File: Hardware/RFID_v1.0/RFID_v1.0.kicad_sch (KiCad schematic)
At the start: 0 parts

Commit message: RFID board schematic done, antenna head created in the layout
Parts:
- added C1, C4: 0.1uF, symbol device:C_Small
- added C10, C9: 180pF, symbol device:C_Small
- added C11, C12: 10pF, symbol device:C_Small
- added C13: 0.1uF, symbol Device:C_Small
- added C2, C3, C7, C8: 15pF, symbol device:C_Small
- added C5, C6: 47pF, symbol device:C_Small
- added J1: Conn_01x08, symbol Connector_Generic:Conn_01x08
- added L1, L2: 2.2uH, symbol Device:L
- added R1: 10k, symbol device:R_US
- added R2: 820R, symbol device:R_US
- added R3: 5k, symbol device:R_US
- added U1: MFRC52202HN1, HVQFN32_5X5_NXP, symbol MFRC52202HN1:MFRC52202HN1
- added Y1: XRCGB27M120F3G00R0, XRCGB27M120F3G00R0:OSC_XRCGB27M120F3G00R0, symbol XRCGB27M120F3G00R0:XRCGB27M120F3G00R0
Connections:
- new net: C4.1, R3.2
- new net: C10.1, C10.2, C11.1, C11.2, C12.1, C12.2, C4.2, C7.2, C8.2, C9.1, C9.2
- new net: C5.2, C7.1, L1.2
- new net: C6.1, C8.1, L2.2
- new net: C2.1, U1.22 (OSCOUT), Y1.3
- new net: C3.1, U1.21 (OSCIN), Y1.1
- new net +3V3: C13.1, J1.1 (Pin_1), R1.1, U1.12 (TVDD), U1.15 (AVDD), U1.2 (PVDD), U1.3 (DVDD), U1.32 (EA), U1.33 (EPAD)
- new net GND: C1.2, C13.2, C2.2, C3.2, C5.1, C6.2, J1.3 (Pin_3), U1.1 (I2C), U1.10 (TVSS), U1.14 (TVSS), U1.18 (AVSS), U1.4 (DVSS), U1.5 (PVSS)
- new net MISO: J1.5 (Pin_5), U1.31 (D7/SCL/MISO/TX)
- new net MOSI: J1.6 (Pin_6), U1.30 (D6/ADR_0/MOSI/MX)
- new net RST: J1.2 (Pin_2), R1.2, U1.6 (NRSTPD)
- new net RX: R2.2, R3.1, U1.17 (RX)
- new net SCK: J1.7 (Pin_7), U1.29 (D5/ADR_1/SCK/DTRQ)
- new net SDA: J1.8 (Pin_8), U1.24 (SDA/NSS/RX)
- new net TX1: L1.1, U1.11 (TX1)
- new net TX2: L2.1, U1.13 (TX2)
- new net Vmid: C1.1, R2.1, U1.16 (VMID)
- no-connect marks 0 -> 11

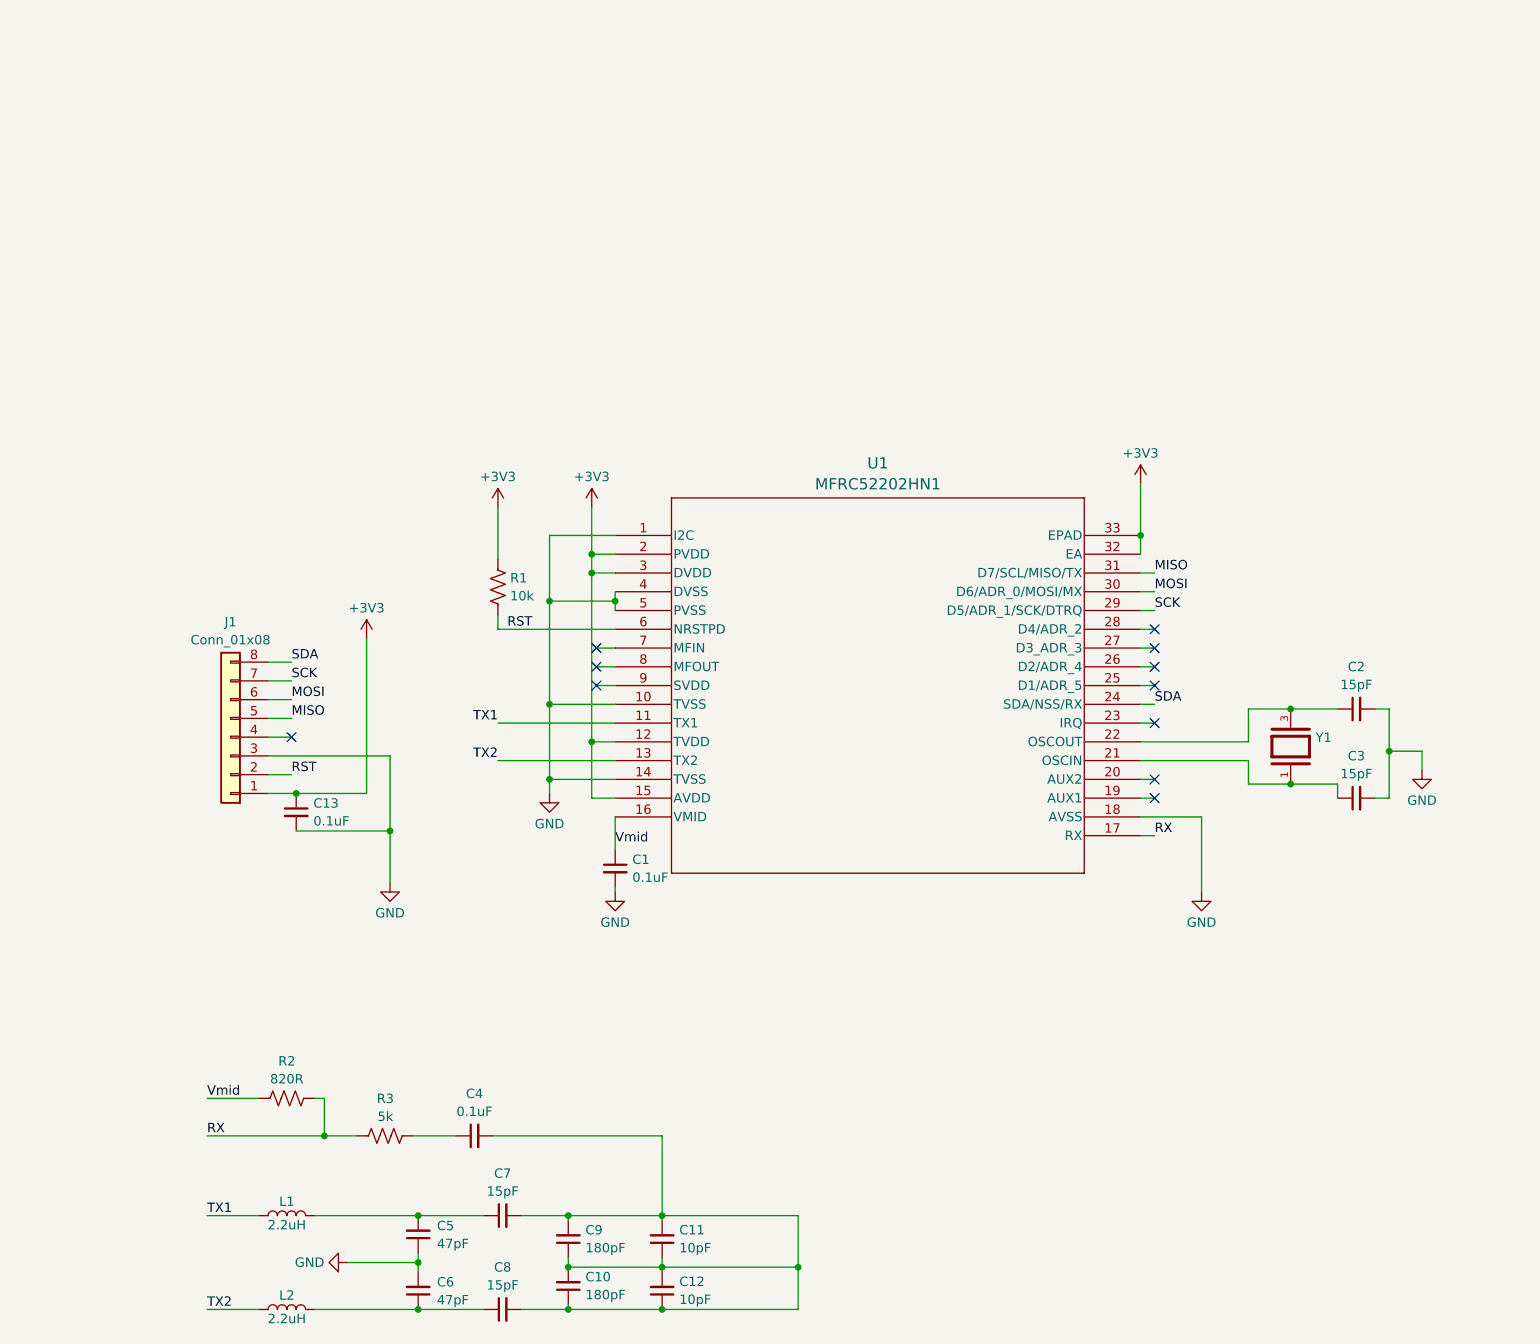
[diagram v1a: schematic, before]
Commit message: RFID schematic done
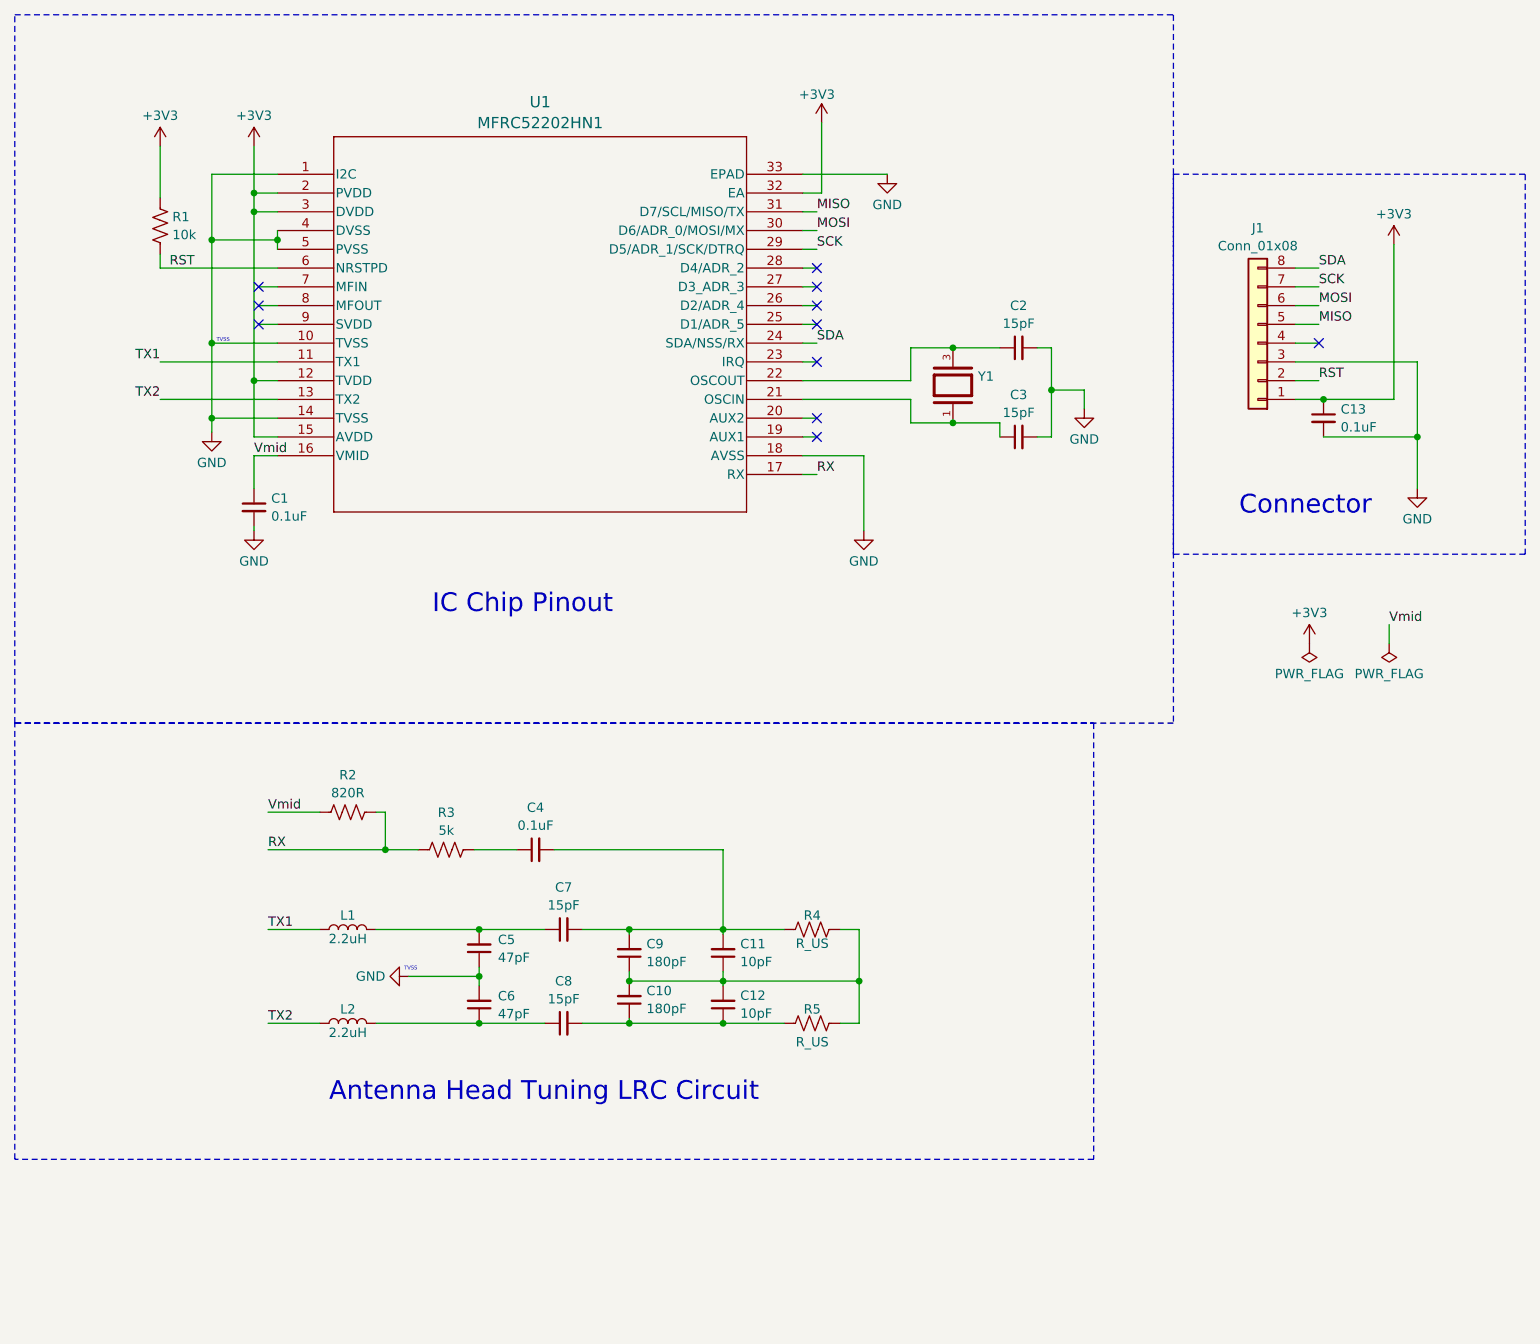
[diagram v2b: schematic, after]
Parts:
- added R4, R5: R_US, symbol device:R_US
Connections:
- net +3V3: no longer U1.33 (EPAD)
- net GND: now also U1.33 (EPAD)
- new net: C10.1, C12.1, C8.2, R5.1
- new net: C10.2, C11.1, C12.2, C9.1, R4.2, R5.2
- new net: C11.2, C4.2, C7.2, C9.2, R4.1
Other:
- note added: "Antenna Head Tuning LRC Circuit"
- note added: "Connector"
- note added: "IC Chip Pinout"
- note added: "TVSS"
- moved on the sheet: C1, C10, C11, C12, C13, C2, C3, C4, C5, C6, C7, C8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
